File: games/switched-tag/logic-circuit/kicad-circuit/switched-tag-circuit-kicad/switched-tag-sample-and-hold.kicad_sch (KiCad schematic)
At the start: 4 parts

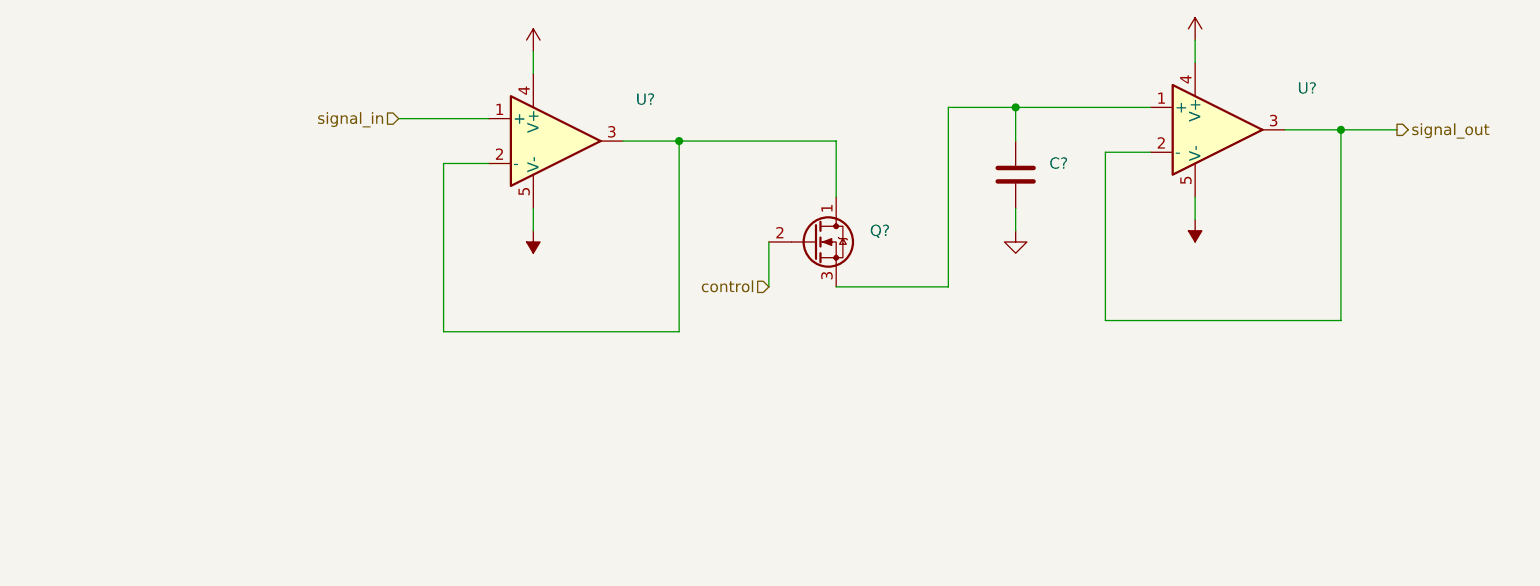
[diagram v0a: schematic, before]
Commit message: Saving progress on kicad schematic. Trying to set up ngspice simulation.
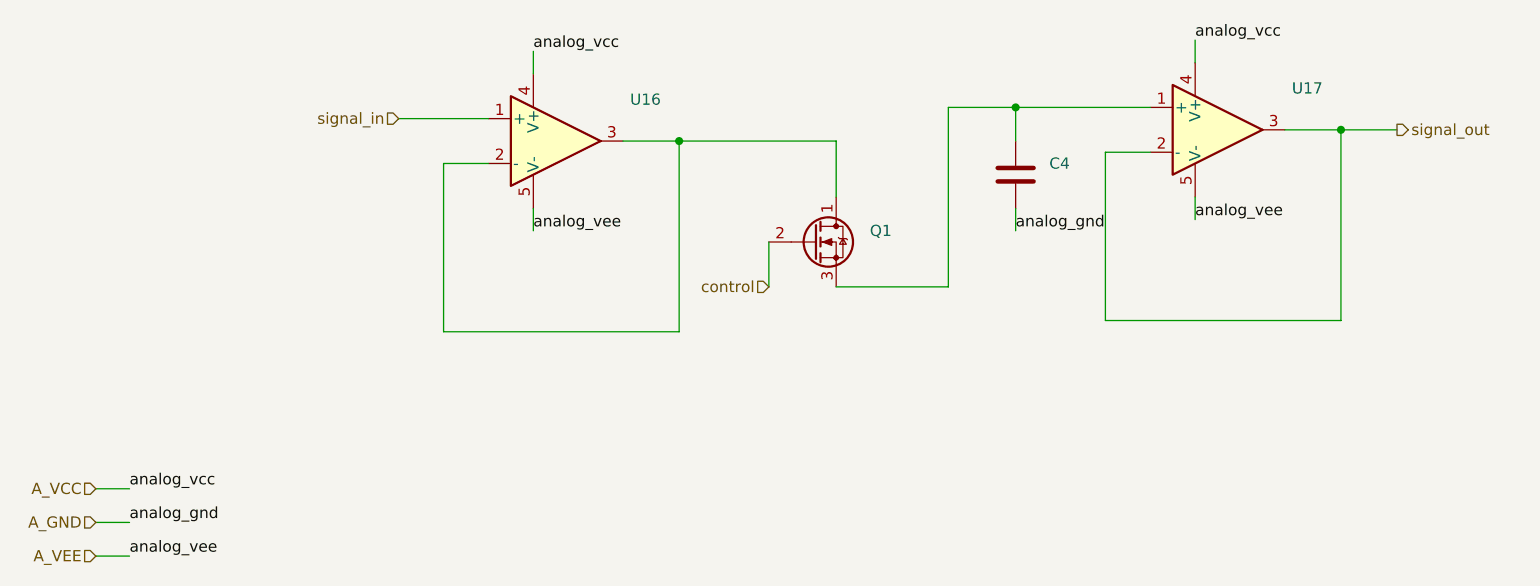
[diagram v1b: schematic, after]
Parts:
- Q1: renamed from Q?; Spice_Lib_File (none) -> /home/pab/Inventions/analog-circuit-game-console/ms-circuit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; Spice_Model (none) -> RUL035N02; Spice_Netlist_Enabled (none) -> Y; Spice_Primitive (none) -> X
- U16: renamed from U?; Spice_Lib_File (none) -> /home/pab/Inventions/analog-circuit-game-console/ms-circuit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; Spice_Model (none) -> LM358; Spice_Node_Sequence (none) -> 1 2 4 5 3
- U17: renamed from U?; value ~ -> (none); Spice_Lib_File (none) -> /home/pab/Inventions/analog-circuit-game-console/ms-circuit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; Spice_Model (none) -> LM358; Spice_Node_Sequence (none) -> 1 2 4 5 3
- gave numbers to parts that had none: 1
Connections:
- net GND renamed A_GND
- net VCC renamed A_VCC
- net VEE renamed A_VEE
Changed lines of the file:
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@@
+    (stroke (width 0) (type default) (color 0 0 0 0))
+  )
+  (wire (pts (xy 66.04 133.35) (xy 69.85 133.35))
     (stroke (width 0) (type default) (color 0 0 0 0))
   )
@@
     (stroke (width 0) (type default) (color 0 0 0 0))
   )
+  (wire (pts (xy 66.04 137.16) (xy 69.85 137.16))
+    (stroke (width 0) (type default) (color 0 0 0 0))
+  )
   (wire (pts (xy 200.66 92.71) (xy 207.01 92.71))
     (stroke (width 0) (type default) (color 0 0 0 0))
@@
     (stroke (width 0) (type default) (color 0 0 0 0))
   )
+  (wire (pts (xy 66.04 140.97) (xy 69.85 140.97))
+    (stroke (width 0) (type default) (color 0 0 0 0))
+  )
   (wire (pts (xy 162.56 110.49) (xy 162.56 90.17))
     (stroke (width 0) (type default) (color 0 0 0 0))
@@
     (stroke (width 0) (type default) (color 0 0 0 0))
   )
+  (label "analog_vcc" (at 115.57 83.82 0)
+    (effects (font (size 1.27 1.27)) (justify left bottom))
+  )
+  (label "analog_vee" (at 115.57 104.14 0)
+    (effects (font (size 1.27 1.27)) (justify left bottom))
+  )
+  (label "analog_gnd" (at 170.18 104.14 0)
+    (effects (font (size 1.27 1.27)) (justify left bottom))
+  )
+  (label "analog_vee" (at 69.85 140.97 0)
+    (effects (font (size 1.27 1.27)) (justify left bottom))
+  )
+  (label "analog_vcc" (at 190.5 82.55 0)
+    (effects (font (size 1.27 1.27)) (justify left bottom))
+  )
+  (label "analog_vee" (at 190.5 102.87 0)
+    (effects (font (size 1.27 1.27)) (justify left bottom))
+  )
+  (label "analog_gnd" (at 69.85 137.16 0)
+    (effects (font (size 1.27 1.27)) (justify left bottom))
+  )
+  (label "analog_vcc" (at 69.85 133.35 0)
+    (effects (font (size 1.27 1.27)) (justify left bottom))
+  )
   (hierarchical_label "signal_in" (shape input) (at 100.33 91.44 180)
+    (effects (font (size 1.27 1.27)) (justify right))
+  )
+  (hierarchical_label "A_VEE" (shape input) (at 66.04 140.97 180)
+    (effects (font (size 1.27 1.27)) (justify right))
+  )
+  (hierarchical_label "A_GND" (shape input) (at 66.04 137.16 180)
     (effects (font (size 1.27 1.27)) (justify right))
   )
@@
     (effects (font (size 1.27 1.27)) (justify left))
   )
+  (hierarchical_label "A_VCC" (shape input) (at 66.04 133.35 180)
+    (effects (font (size 1.27 1.27)) (justify right))
+  )
   (hierarchical_label "control" (shape input) (at 142.24 110.49 180)
     (effects (font (size 1.27 1.27)) (justify right))
   )
-  (symbol (lib_id "power:VCC") (at 115.57 83.82 0) (unit 1)
-    (in_bom yes) (on_board yes) (fields_autoplaced)
-    (property "Reference" "#PWR?" (id 0) (at 115.57 87.63 0)
-      (effects (font (size 1.27 1.27)) hide)
-    )
-    (property "Value" "" (id 1) (at 115.57 78.74 0))
-    (property "Footprint" "" (id 2) (at 115.57 83.82 0)
-      (effects (font (size 1.27 1.27)) hide)
-    )
-    (property "Datasheet" "" (id 3) (at 115.57 83.82 0)
-      (effects (font (size 1.27 1.27)) hide)
-    )
-    (pin "1")
-  )
   (symbol (lib_id "Simulation_SPICE:OPAMP") (at 193.04 92.71 0) (unit 1)
     (in_bom yes) (on_board yes) (fields_autoplaced)
-    (property "Reference" "U?" (id 0) (at 203.2 88.011 0))
-    (property "Value" "~" (id 1) (at 203.2 90.551 0))
+    (property "Reference" "U17" (id 0) (at 203.2 88.011 0))
+    (property "Value" "" (id 1) (at 203.2 90.551 0))
     (property "Footprint" "" (id 2) (at 193.04 92.71 0)
       (effects (font (size 1.27 1.27)) hide)
@@
     (property "Spice_Primitive" "X" (id 5) (at 193.04 92.71 0)
       (effects (font (size 1.27 1.27)) (justify left) hide)
+    )
+    (property "Spice_Model" "LM358" (id 6) (at 193.04 92.71 0)
+      (effects (font (size 1.27 1.27)) hide)
+    )
+    (property "Spice_Lib_File" "/home/pab/Inventions/analog-circuit-game-console/ms-circuit-video-games/spice-models/LM358-onsemi.mod" (id 7) (at 193.04 92.71 0)
+      (effects (font (size 1.27 1.27)) hide)
+    )
+    (property "Spice_Node_Sequence" "1 2 4 5 3" (id 8) (at 193.04 92.71 0)
+      (effects (font (size 1.27 1.27)) hide)
     )
     (pin "1")
@@
   (symbol (lib_id "Simulation_SPICE:OPAMP") (at 118.11 93.98 0) (unit 1)
     (in_bom yes) (on_board yes) (fields_autoplaced)
-    (property "Reference" "U?" (id 0) (at 128.27 89.281 0))
+    (property "Reference" "U16" (id 0) (at 128.27 89.281 0))
     (property "Value" "" (id 1) (at 128.27 91.821 0))
     (property "Footprint" "" (id 2) (at 118.11 93.98 0)
@@
     (property "Spice_Primitive" "X" (id 5) (at 118.11 93.98 0)
       (effects (font (size 1.27 1.27)) (justify left) hide)
+    )
+    (property "Spice_Model" "LM358" (id 6) (at 118.11 93.98 0)
+      (effects (font (size 1.27 1.27)) hide)
+    )
+    (property "Spice_Lib_File" "/home/pab/Inventions/analog-circuit-game-console/ms-circuit-video-games/spice-models/LM358-onsemi.mod" (id 7) (at 118.11 93.98 0)
+      (effects (font (size 1.27 1.27)) hide)
+    )
+    (property "Spice_Node_Sequence" "1 2 4 5 3" (id 8) (at 118.11 93.98 0)
+      (effects (font (size 1.27 1.27)) hide)
     )
     (pin "1")
@@
     (pin "5")
   )
-  (symbol (lib_id "power:GND") (at 170.18 104.14 0) (unit 1)
-    (in_bom yes) (on_board yes) (fields_autoplaced)
-    (property "Reference" "#PWR?" (id 0) (at 170.18 110.49 0)
-      (effects (font (size 1.27 1.27)) hide)
-    )
-    (property "Value" "" (id 1) (at 170.18 109.22 0))
-    (property "Footprint" "" (id 2) (at 170.18 104.14 0)
-      (effects (font (size 1.27 1.27)) hide)
-    )
-    (property "Datasheet" "" (id 3) (at 170.18 104.14 0)
-      (effects (font (size 1.27 1.27)) hide)
-    )
-    (pin "1")
-  )
   (symbol (lib_id "Device:Q_NMOS_DGS") (at 147.32 105.41 0) (unit 1)
     (in_bom yes) (on_board yes) (fields_autoplaced)
-    (property "Reference" "Q?" (id 0) (at 153.67 104.1399 0)
+    (property "Reference" "Q1" (id 0) (at 153.67 104.1399 0)
       (effects (font (size 1.27 1.27)) (justify left))
     )
@@
       (effects (font (size 1.27 1.27)) hide)
     )
+    (property "Spice_Primitive" "X" (id 4) (at 147.32 105.41 0)
+      (effects (font (size 1.27 1.27)) hide)
+    )
+    (property "Spice_Model" "RUL035N02" (id 5) (at 147.32 105.41 0)
+      (effects (font (size 1.27 1.27)) hide)
+    )
+    (property "Spice_Netlist_Enabled" "Y" (id 6) (at 147.32 105.41 0)
+      (effects (font (size 1.27 1.27)) hide)
+    )
+    (property "Spice_Lib_File" "/home/pab/Inventions/analog-circuit-game-console/ms-circuit-video-games/spice-models/rul035n02.lib" (id 7) (at 147.32 105.41 0)
+      (effects (font (size 1.27 1.27)) hide)
+    )
     (pin "1")
     (pin "2")
     (pin "3")
   )
-  (symbol (lib_id "power:VCC") (at 190.5 82.55 0) (unit 1)
-    (in_bom yes) (on_board yes) (fields_autoplaced)
-    (property "Reference" "#PWR?" (id 0) (at 190.5 86.36 0)
-      (effects (font (size 1.27 1.27)) hide)
-    )
-    (property "Value" "" (id 1) (at 190.5 77.47 0))
-    (property "Footprint" "" (id 2) (at 190.5 82.55 0)
-      (effects (font (size 1.27 1.27)) hide)
-    )
-    (property "Datasheet" "" (id 3) (at 190.5 82.55 0)
-      (effects (font (size 1.27 1.27)) hide)
-    )
-    (pin "1")
-  )
   (symbol (lib_id "Device:C") (at 170.18 97.79 0) (unit 1)
     (in_bom yes) (on_board yes) (fields_autoplaced)
-    (property "Reference" "C?" (id 0) (at 173.99 96.5199 0)
+    (property "Reference" "C4" (id 0) (at 173.99 96.5199 0)
       (effects (font (size 1.27 1.27)) (justify left))
     )
@@
     (pin "2")
   )
-  (symbol (lib_id "power:VEE") (at 190.5 102.87 180) (unit 1)
-    (in_bom yes) (on_board yes) (fields_autoplaced)
-    (property "Reference" "#PWR?" (id 0) (at 190.5 99.06 0)
-      (effects (font (size 1.27 1.27)) hide)
-    )
-    (property "Value" "" (id 1) (at 190.5 107.95 0))
-    (property "Footprint" "" (id 2) (at 190.5 102.87 0)
-      (effects (font (size 1.27 1.27)) hide)
-    )
-    (property "Datasheet" "" (id 3) (at 190.5 102.87 0)
-      (effects (font (size 1.27 1.27)) hide)
-    )
-    (pin "1")
-  )
-  (symbol (lib_id "power:VEE") (at 115.57 104.14 180) (unit 1)
-    (in_bom yes) (on_board yes) (fields_autoplaced)
-    (property "Reference" "#PWR?" (id 0) (at 115.57 100.33 0)
-      (effects (font (size 1.27 1.27)) hide)
-    )
-    (property "Value" "" (id 1) (at 115.57 109.22 0))
-    (property "Footprint" "" (id 2) (at 115.57 104.14 0)
-      (effects (font (size 1.27 1.27)) hide)
-    )
-    (property "Datasheet" "" (id 3) (at 115.57 104.14 0)
-      (effects (font (size 1.27 1.27)) hide)
-    )
-    (pin "1")
-  )
 )

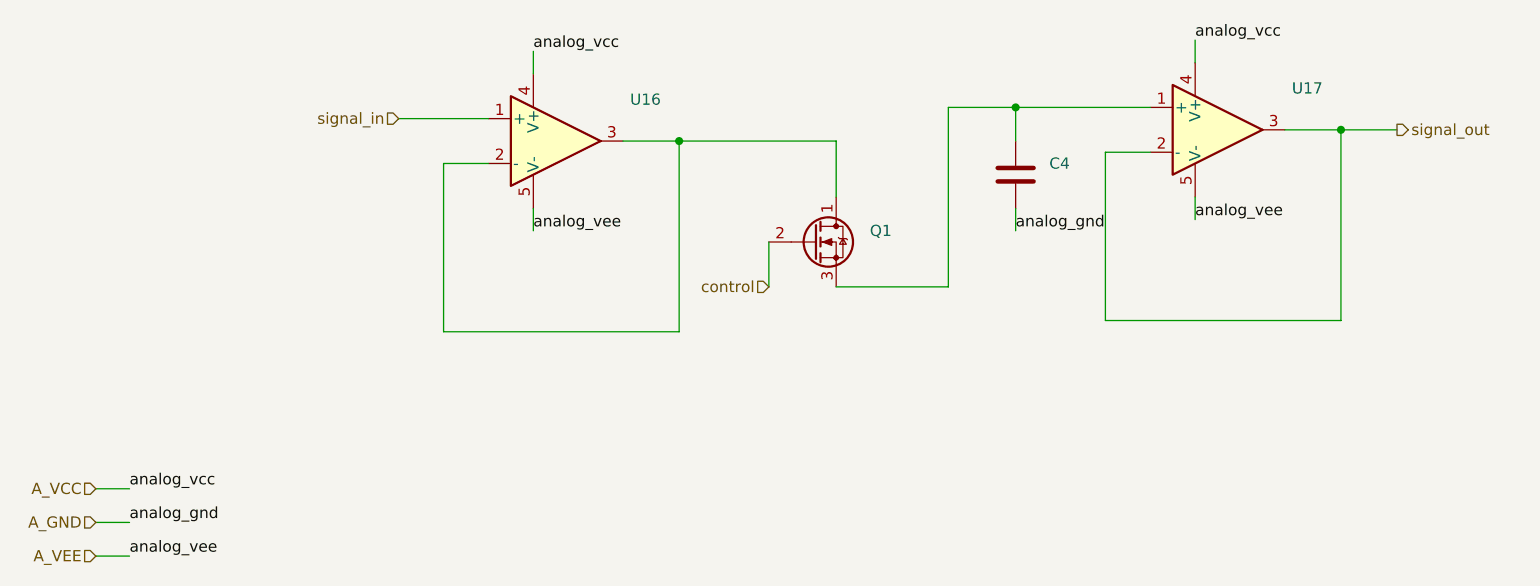
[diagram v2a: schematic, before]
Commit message: Changed spice model of opamp in kicad sim. Fixed design error in it player determination in ltspice and kicad schematic
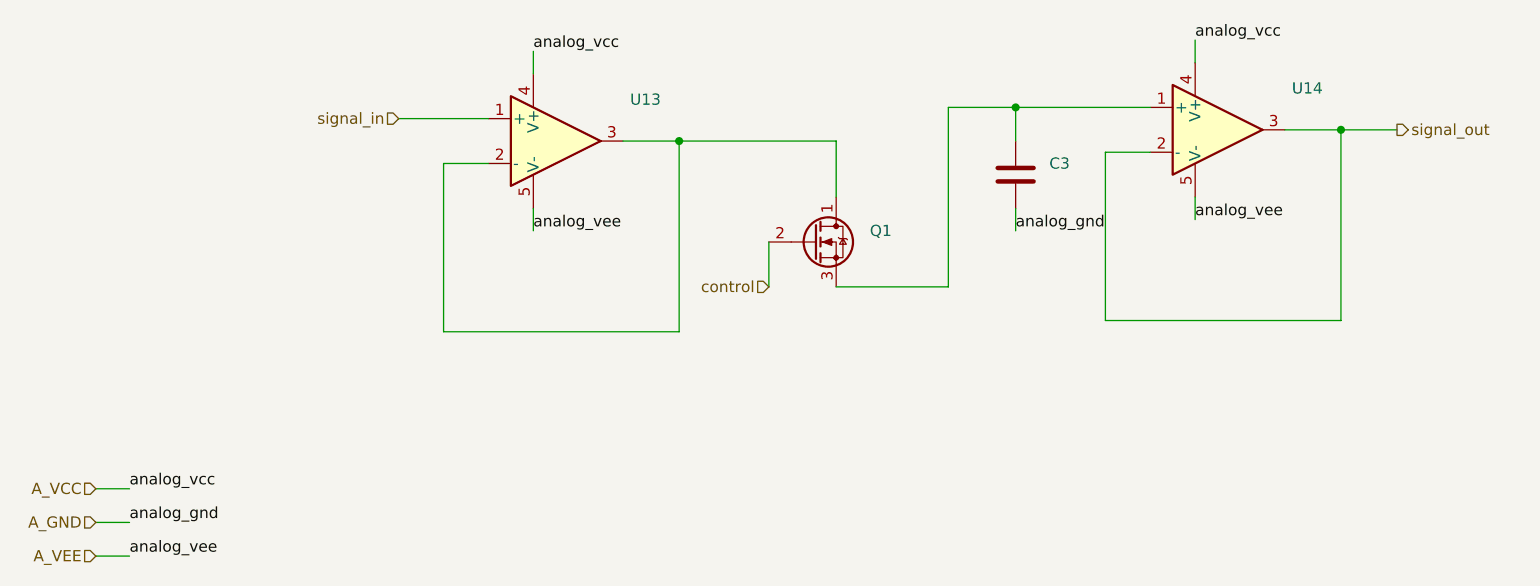
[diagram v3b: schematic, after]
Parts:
- U13: renamed from U16; Spice_Lib_File /home/pab/Inventions/analog-circuit-game-console/ms-circuit-video-games/spice-models/LM358-onsemi.mod -> /home/pab/Inventions/analog-circuit-game-console/ms-circuit-video-games/spice-models/ada4692.mod; Spice_Model LM358 -> ADA4692
- U14: renamed from U17; Spice_Lib_File /home/pab/Inventions/analog-circuit-game-console/ms-circuit-video-games/spice-models/LM358-onsemi.mod -> /home/pab/Inventions/analog-circuit-game-console/ms-circuit-video-games/spice-models/ada4692.mod; Spice_Model LM358 -> ADA4692
- renumbered C4 to C3
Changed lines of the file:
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@@
   (symbol (lib_id "Simulation_SPICE:OPAMP") (at 193.04 92.71 0) (unit 1)
     (in_bom yes) (on_board yes) (fields_autoplaced)
-    (property "Reference" "U17" (id 0) (at 203.2 88.011 0))
+    (property "Reference" "U14" (id 0) (at 203.2 88.011 0))
     (property "Value" "" (id 1) (at 203.2 90.551 0))
     (property "Footprint" "" (id 2) (at 193.04 92.71 0)
@@
       (effects (font (size 1.27 1.27)) (justify left) hide)
     )
-    (property "Spice_Model" "LM358" (id 6) (at 193.04 92.71 0)
+    (property "Spice_Model" "ADA4692" (id 6) (at 193.04 92.71 0)
       (effects (font (size 1.27 1.27)) hide)
     )
-    (property "Spice_Lib_File" "/home/pab/Inventions/analog-circuit-game-console/ms-circuit-video-games/spice-models/LM358-onsemi.mod" (id 7) (at 193.04 92.71 0)
+    (property "Spice_Lib_File" "/home/pab/Inventions/analog-circuit-game-console/ms-circuit-video-games/spice-models/ada4692.mod" (id 7) (at 193.04 92.71 0)
       (effects (font (size 1.27 1.27)) hide)
     )
@@
   (symbol (lib_id "Simulation_SPICE:OPAMP") (at 118.11 93.98 0) (unit 1)
     (in_bom yes) (on_board yes) (fields_autoplaced)
-    (property "Reference" "U16" (id 0) (at 128.27 89.281 0))
+    (property "Reference" "U13" (id 0) (at 128.27 89.281 0))
     (property "Value" "" (id 1) (at 128.27 91.821 0))
     (property "Footprint" "" (id 2) (at 118.11 93.98 0)
@@
       (effects (font (size 1.27 1.27)) (justify left) hide)
     )
-    (property "Spice_Model" "LM358" (id 6) (at 118.11 93.98 0)
+    (property "Spice_Model" "ADA4692" (id 6) (at 118.11 93.98 0)
       (effects (font (size 1.27 1.27)) hide)
     )
-    (property "Spice_Lib_File" "/home/pab/Inventions/analog-circuit-game-console/ms-circuit-video-games/spice-models/LM358-onsemi.mod" (id 7) (at 118.11 93.98 0)
+    (property "Spice_Lib_File" "/home/pab/Inventions/analog-circuit-game-console/ms-circuit-video-games/spice-models/ada4692.mod" (id 7) (at 118.11 93.98 0)
       (effects (font (size 1.27 1.27)) hide)
     )
@@
   (symbol (lib_id "Device:C") (at 170.18 97.79 0) (unit 1)
     (in_bom yes) (on_board yes) (fields_autoplaced)
-    (property "Reference" "C4" (id 0) (at 173.99 96.5199 0)
+    (property "Reference" "C3" (id 0) (at 173.99 96.5199 0)
       (effects (font (size 1.27 1.27)) (justify left))
     )

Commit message: Updated kicad circuit. The kicad sim and ltspice do not match up well. Need to fix.
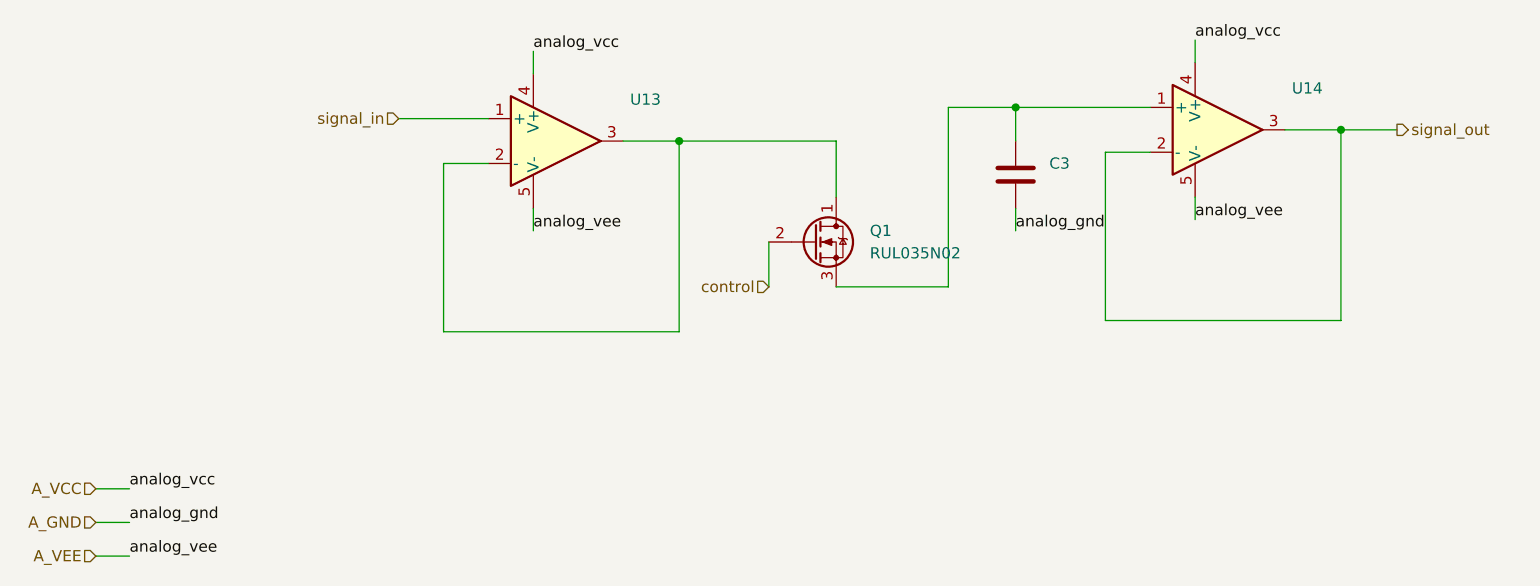
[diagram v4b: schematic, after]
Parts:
- Q1: value (none) -> RUL035N02
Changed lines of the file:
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@@
       (effects (font (size 1.27 1.27)) (justify left))
     )
-    (property "Value" "" (id 1) (at 153.67 106.6799 0)
+    (property "Value" "RUL035N02" (id 1) (at 153.67 106.6799 0)
       (effects (font (size 1.27 1.27)) (justify left))
     )
